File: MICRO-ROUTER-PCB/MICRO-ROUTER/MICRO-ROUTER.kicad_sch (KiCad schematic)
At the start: 5 parts, among them J1 Conn_01x02_Pin

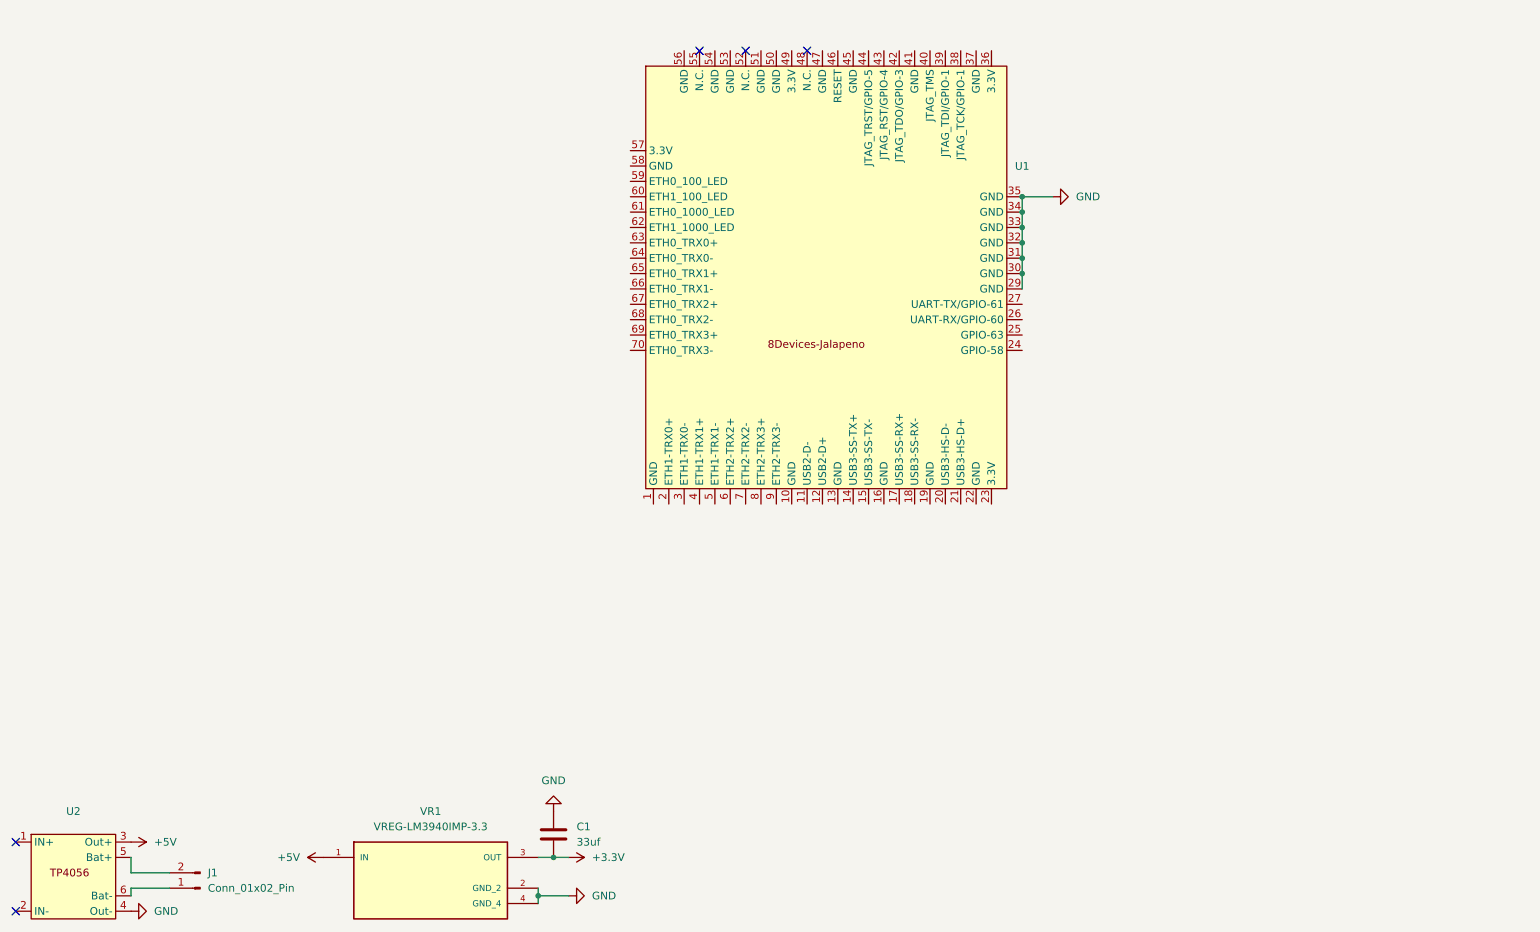
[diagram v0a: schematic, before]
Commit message: Added USB 3.0 Started adding onboard URAT to TTL
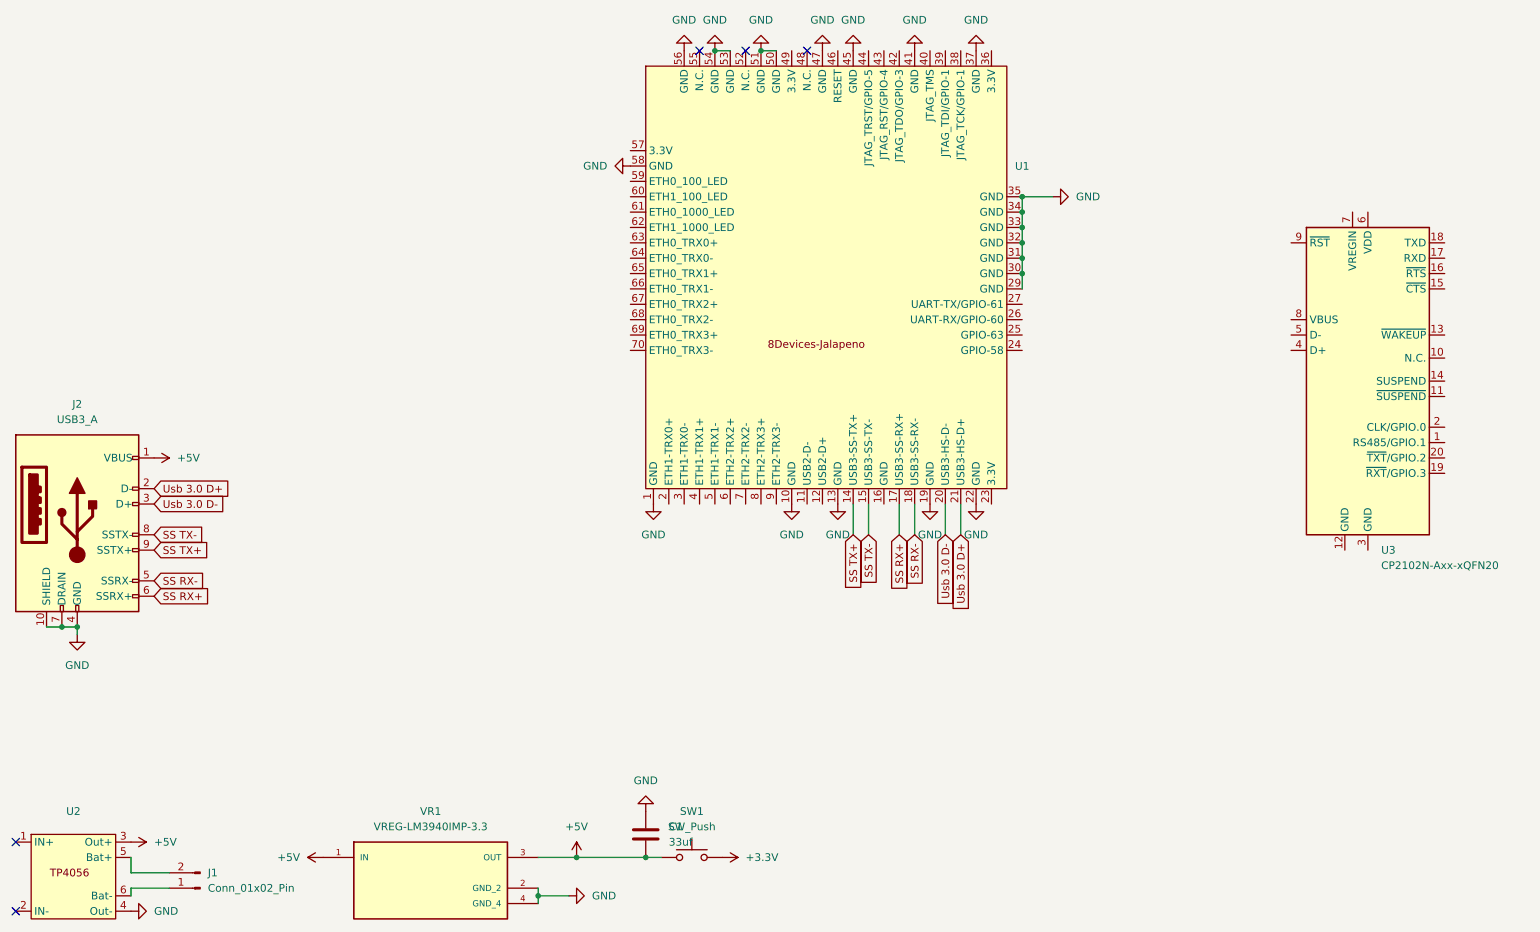
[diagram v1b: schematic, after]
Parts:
- added J2: USB3_A, symbol Connector:USB3_A
- added SW1: SW_Push, symbol Switch:SW_Push
- added U3: CP2102N-Axx-xQFN20, Package_DFN_QFN:SiliconLabs_QFN-20-1EP_3x3mm_P0.5mm, symbol Interface_USB:CP2102N-Axx-xQFN20
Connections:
- net +3.3V: now also SW1.2; no longer C1.2, VR1.3 (OUT)
- net +5V: now also C1.2, VR1.3 (OUT), J2.1 (VBUS), SW1.1
- net GND: now also U1.1 (GND), U1.10 (GND), U1.13 (GND), U1.19 (GND), U1.22 (GND), U1.37 (GND), U1.41 (GND), U1.45 (GND), U1.47 (GND), U1.50 (GND), U1.51 (GND), U1.53 (GND), U1.54 (GND), U1.56 (GND), U1.58 (GND), J2.10 (SHIELD), J2.4 (GND), J2.7 (DRAIN)
- net SS TX+: now reaches U1.14 (USB3-SS-TX+)
- net SS TX+: now also J2.9 (SSTX+)
- net SS TX-: now reaches U1.15 (USB3-SS-TX-)
- net SS TX-: now also J2.8 (SSTX-)
- net SS RX+: now reaches U1.17 (USB3-SS-RX+)
- net SS RX+: now also J2.6 (SSRX+)
- net SS RX-: now reaches U1.18 (USB3-SS-RX-)
- net SS RX-: now also J2.5 (SSRX-)
- net Usb 3.0 D-: now reaches U1.20 (USB3-HS-D-)
- net Usb 3.0 D-: now also J2.3 (D+)
- net Usb 3.0 D+: now reaches U1.21 (USB3-HS-D+)
- net Usb 3.0 D+: now also J2.2 (D-)
- new net: U3.12 (GND), U3.21 (GND), U3.3 (GND)
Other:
- moved on the sheet: C1

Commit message: routine back up
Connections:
- net GND: now also U3.12 (GND), U3.21 (GND), U3.3 (GND)
- net URAT-TX: now reaches U3.17 (RXD)
- net URAT-TX: now also U1.27 (UART-TX/GPIO-61)
- net URAT-RX: now reaches U3.18 (TXD)
- net URAT-RX: now also U1.26 (UART-RX/GPIO-60)
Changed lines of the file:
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@@
 	(paper "A4")
+	(junction
+		(at 238.76 125.73)
+		(diameter 0)
+		(color 0 0 0 0)
+	)
 	(junction
 		(at 27.94 138.43)
@@
 	(wire
 		(pts
+			(xy 238.76 125.73) (xy 241.3 125.73)
+		)
+		(stroke
+			(width 0)
+			(type default)
+		)
+	)
+	(wire
+		(pts
 			(xy 110.49 176.53) (xy 121.92 176.53)
 		)
@@
 		(pts
 			(xy 36.83 179.07) (xy 36.83 176.53)
+		)
+		(stroke
+			(width 0)
+			(type default)
+		)
+	)
+	(wire
+		(pts
+			(xy 237.49 125.73) (xy 238.76 125.73)
 		)
 		(stroke
@@
 		)
 	)
+	(global_label "URAT-RX"
+		(shape input)
+		(at 184.15 87.63 0)
+		(fields_autoplaced yes)
+		(effects
+			(font
+				(size 1.27 1.27)
+			)
+			(justify left)
+		)
+		(property "Intersheetrefs" "${INTERSHEET_REFS}"
+			(at 195.8438 87.63 0)
+			(effects
+				(font
+					(size 1.27 1.27)
+				)
+				(justify left)
+				(hide yes)
+			)
+		)
+	)
 	(global_label "SS RX-"
 		(shape input)
@@
 		)
 	)
+	(global_label "URAT-TX"
+		(shape input)
+		(at 254 77.47 0)
+		(fields_autoplaced yes)
+		(effects
+			(font
+				(size 1.27 1.27)
+			)
+			(justify left)
+		)
+		(property "Intersheetrefs" "${INTERSHEET_REFS}"
+			(at 265.3914 77.47 0)
+			(effects
+				(font
+					(size 1.27 1.27)
+				)
+				(justify left)
+				(hide yes)
+			)
+		)
+	)
+	(global_label "URAT-RX"
+		(shape input)
+		(at 254 74.93 0)
+		(fields_autoplaced yes)
+		(effects
+			(font
+				(size 1.27 1.27)
+			)
+			(justify left)
+		)
+		(property "Intersheetrefs" "${INTERSHEET_REFS}"
+			(at 265.6938 74.93 0)
+			(effects
+				(font
+					(size 1.27 1.27)
+				)
+				(justify left)
+				(hide yes)
+			)
+		)
+	)
 	(global_label "SS RX+"
 		(shape input)
@@
 				)
 				(justify right)
+				(hide yes)
+			)
+		)
+	)
+	(global_label "URAT-TX"
+		(shape input)
+		(at 184.15 85.09 0)
+		(fields_autoplaced yes)
+		(effects
+			(font
+				(size 1.27 1.27)
+			)
+			(justify left)
+		)
+		(property "Intersheetrefs" "${INTERSHEET_REFS}"
+			(at 195.5414 85.09 0)
+			(effects
+				(font
+					(size 1.27 1.27)
+				)
+				(justify left)
 				(hide yes)
 			)
@@
 					(unit 1)
 				)
+			)
+		)
+	)
+	(symbol
+		(lib_id "power:GND")
+		(at 238.76 125.73 0)
+		(unit 1)
+		(exclude_from_sim no)
+		(in_bom yes)
+		(on_board yes)
+		(dnp no)
+		(fields_autoplaced yes)
+		(property "Reference" "#PWR024"
+			(at 238.76 132.08 0)
+			(effects
+				(font
+					(size 1.27 1.27)
+				)
+				(hide yes)
+			)
+		)
+		(property "Value" "GND"
+			(at 238.76 130.81 0)
+			(effects
+				(font
+					(size 1.27 1.27)
+				)
+			)
+		)
+		(property "Footprint" ""
+			(at 238.76 125.73 0)
+			(effects
+				(font
+					(size 1.27 1.27)
+				)
+				(hide yes)
+			)
+		)
+		(property "Datasheet" ""
+			(at 238.76 125.73 0)
+			(effects
+				(font
+					(size 1.27 1.27)
+				)
+				(hide yes)
+			)
+		)
+		(property "Description" "Power symbol creates a global label with name \"GND\" , ground"
+			(at 238.76 125.73 0)
+			(effects
+				(font
+					(size 1.27 1.27)
+				)
+				(hide yes)
+			)
+		)
+		(pin "1"
+		)
+		(instances
+			(project "MICRO-ROUTER"
+				(path "/ebd99a91-a0ff-4b6f-9899-bd1b2d3fbcb2"
+					(reference "#PWR024")
+					(unit 1)
+				)

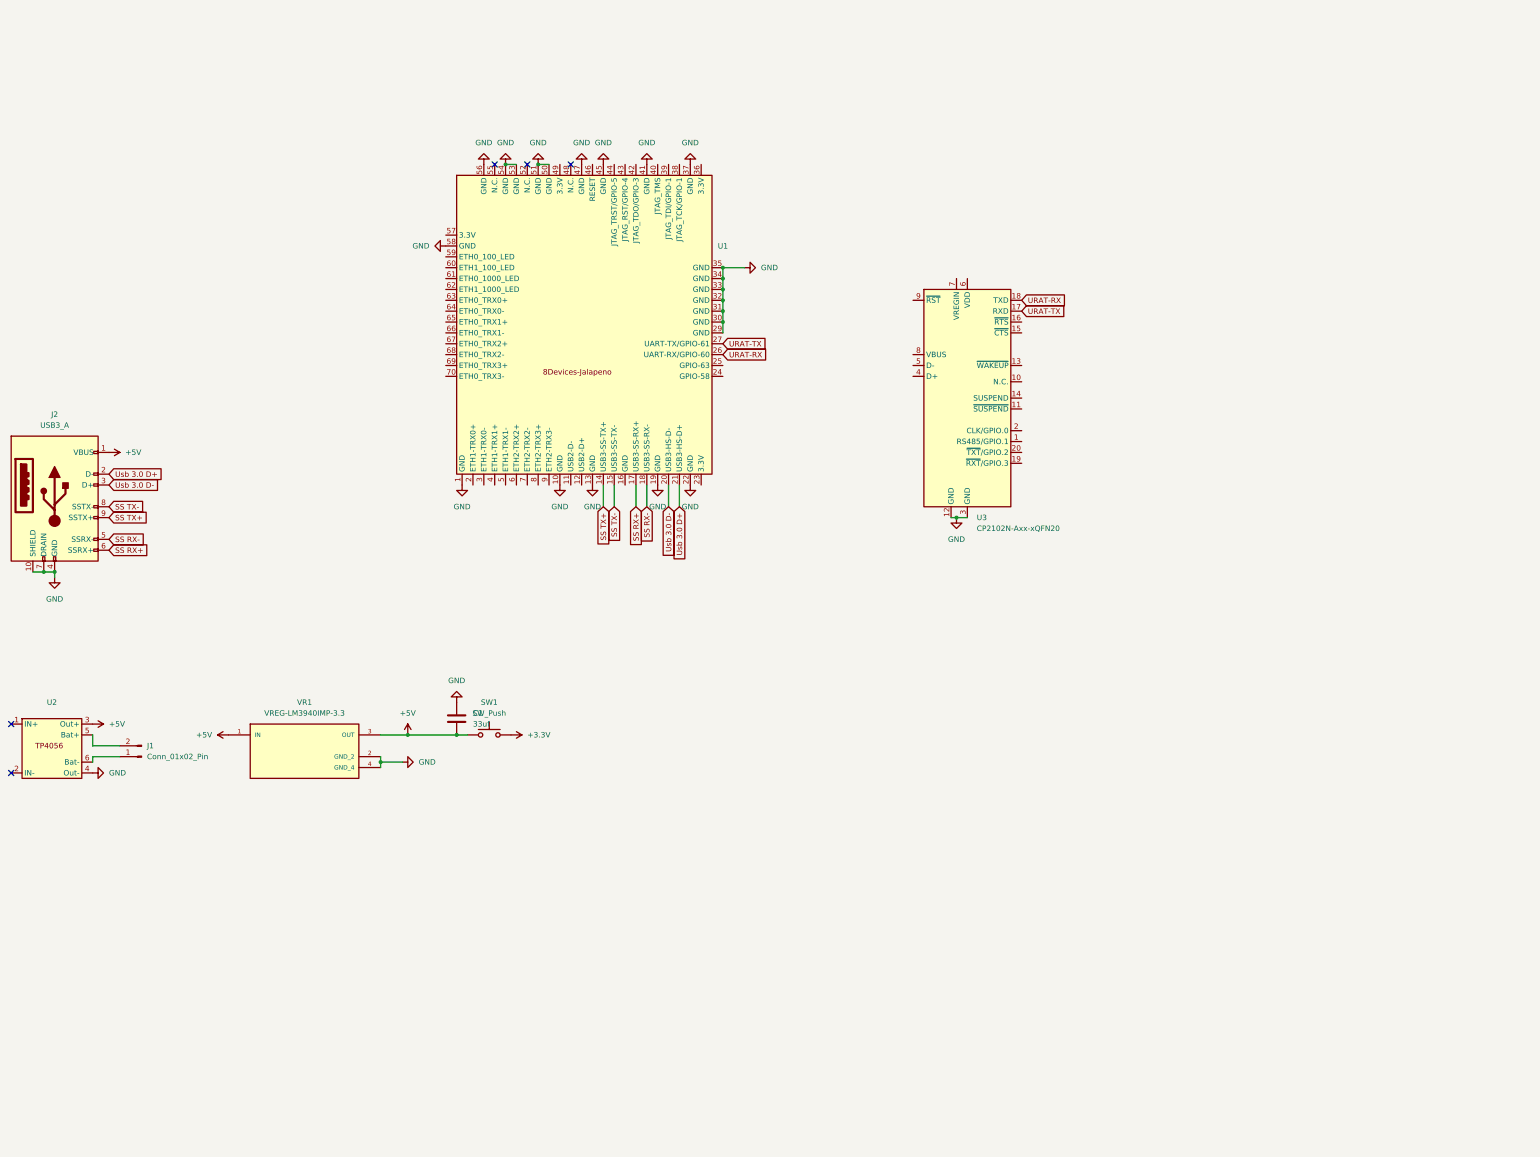
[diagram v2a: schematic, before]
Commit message: Swapped SOM due to lower wattage Worked on scematic -UART IC -USB C PORT -USB 2.0 PORT
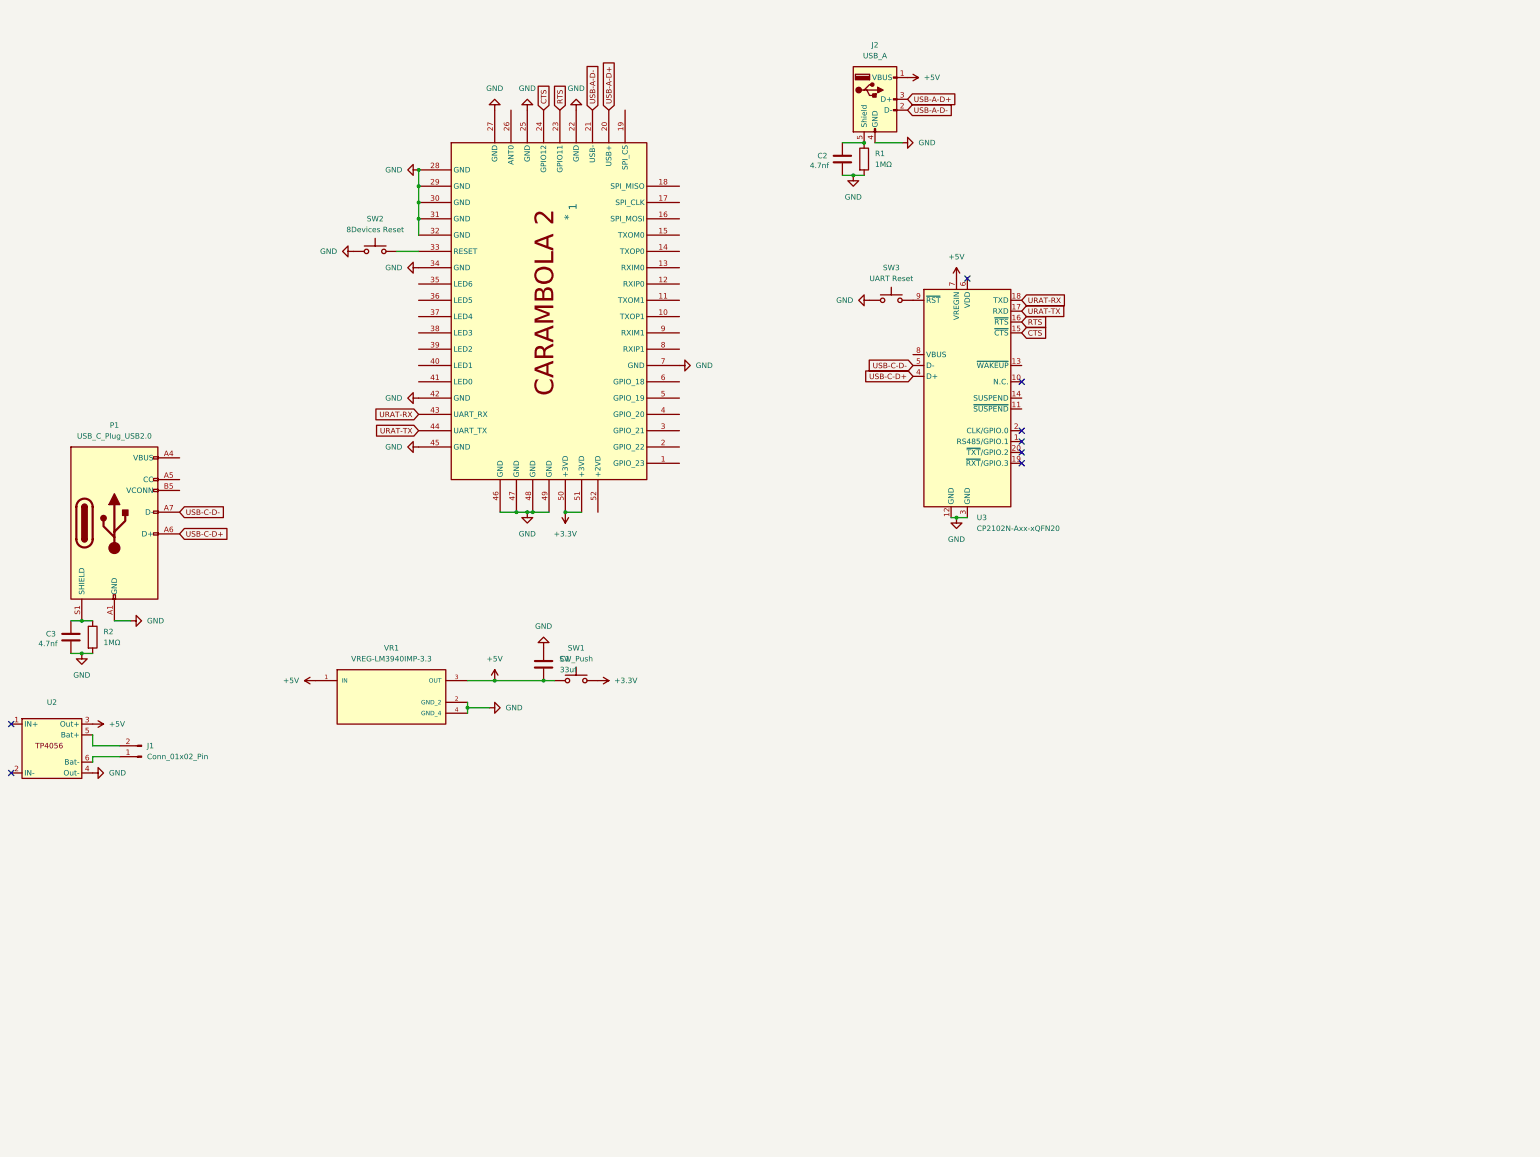
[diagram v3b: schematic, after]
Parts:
- removed J2: USB3_A, symbol Connector:USB3_A
- removed U1: ~, symbol Custom Symbols:8Devices-Jalapeno
- added 1: *, symbol Custom Symbols:8Devices-Carambola 2
- added C2, C3: 4.7nf, symbol Device:C
- added J2: USB_A, symbol Connector:USB_A
- added P1: USB_C_Plug_USB2.0, symbol Connector:USB_C_Plug_USB2.0
- added R1, R2: 1MΩ, symbol Device:R
- added SW2: 8Devices Reset, symbol Switch:SW_Push
- added SW3: UART Reset, symbol Switch:SW_Push
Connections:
- net +3.3V: now also 1.50 (+3VD), 1.51 (+3VD)
- net +5V: now also U3.7 (VREGIN), J2.1 (VBUS)
- net GND: now also 1.22 (GND), 1.25 (GND), 1.27 (GND), 1.28 (GND), 1.29 (GND), 1.30 (GND), 1.31 (GND), 1.32 (GND), 1.34 (GND), 1.42 (GND), 1.45 (GND), 1.46 (GND), 1.47 (GND), 1.48 (GND), 1.49 (GND), 1.7 (GND), C2.2, C3.2, J2.4 (GND), P1.A1 (GND), P1.A12 (GND), P1.B1 (GND), P1.B12 (GND), R1.2, R2.2, SW2.1, SW3.1
- net URAT-RX: now also 1.43 (UART_RX)
- net URAT-TX: now also 1.44 (UART_TX)
- net CTS: now reaches U3.15 (~{CTS})
- net CTS: now also 1.24 (GPIO12)
- net RTS: now reaches U3.16 (~{RTS})
- net RTS: now also 1.23 (GPIO11)
- net USB-C-D+: now reaches U3.4 (D+)
- net USB-C-D+: now also P1.A6 (D+)
- net USB-C-D-: now reaches U3.5 (D-)
- net USB-C-D-: now also P1.A7 (D-)
- net at U3.9 (~{RST}): now also SW3.2
- new net: P1.A4 (VBUS), P1.A9 (VBUS), P1.B4 (VBUS), P1.B9 (VBUS)
- new net: C3.1, P1.S1 (SHIELD), R2.1
- new net: C2.1, J2.5 (Shield), R1.1
- new net: 1.33 (RESET), SW2.2
- new net USB-A-D+: 1.20 (USB+), J2.3 (D+)
- new net USB-A-D-: 1.21 (USB-), J2.2 (D-)
- no-connect marks 5 -> 8
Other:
- moved on the sheet: C1, SW1, VR1
